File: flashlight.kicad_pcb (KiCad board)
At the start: 2 copper layers, 45 x 120 mm, 23 parts, among them J1 USB_B_Micro, J2 Conn_01x03_Pin, Q2 HSS2333, SW1 SW_DIP_x01, U1 XB4908A, U2 MT3608, U3 TP4057, U4 R6BHC-A05_LED-19-223

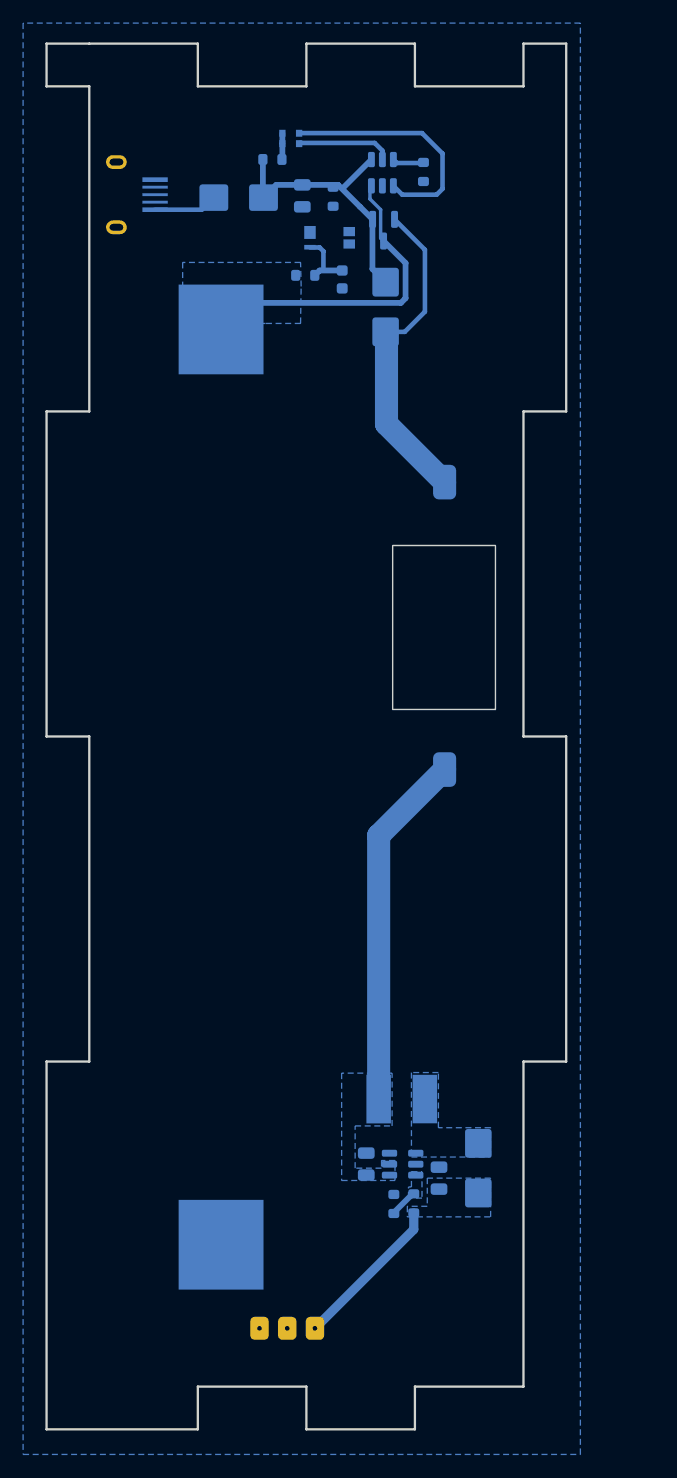
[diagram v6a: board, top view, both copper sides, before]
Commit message: increased 18650 pads size, added led stripe silkscreen line, increased switch hole length by 0.1mm
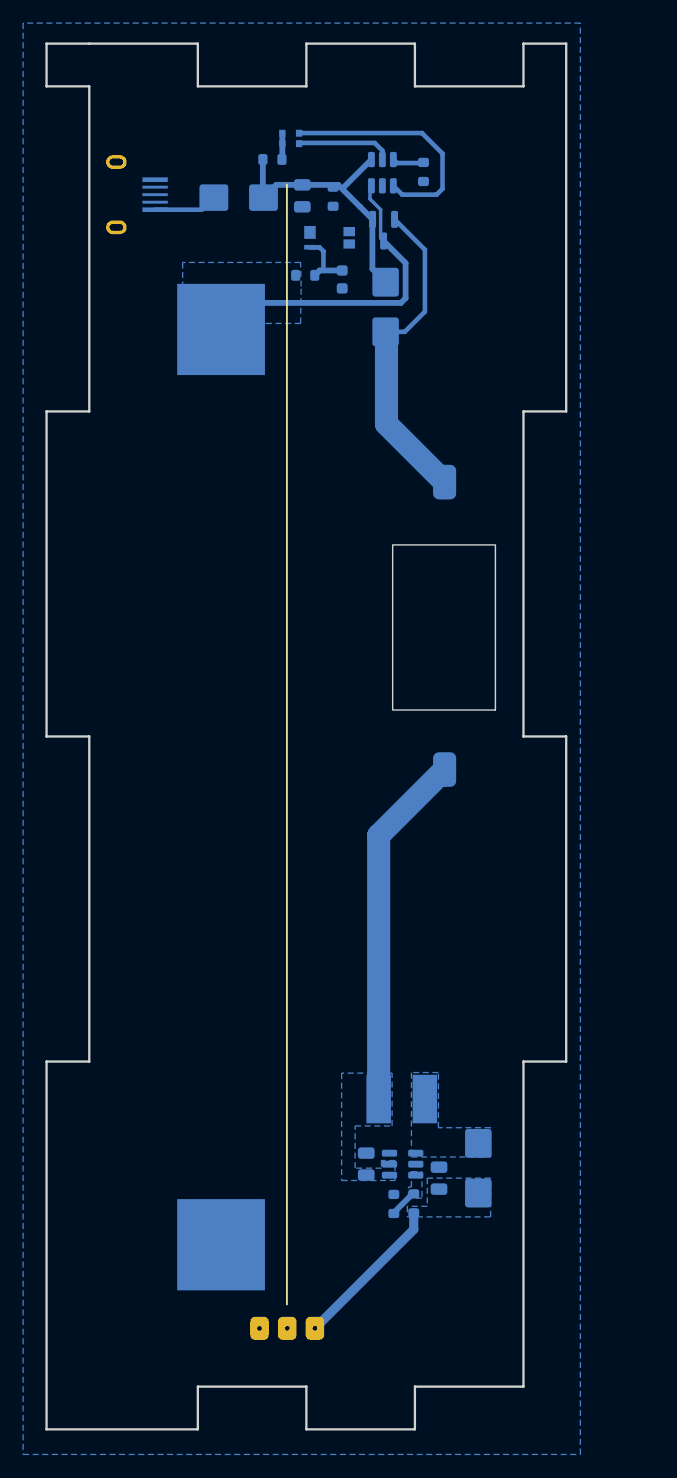
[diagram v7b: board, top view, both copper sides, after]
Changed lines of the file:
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@@
 		)
 		(fp_rect
-			(start 14.1 -8.9)
-			(end -0.1 0)
+			(start 14.15 -8.9)
+			(end -0.15 0)
 			(stroke
 				(width 0.12)
@@
 		(pad "1" smd rect
 			(at 0 -39.63 270)
-			(size 7.77 7.35)
+			(size 7.9 7.6)
 			(layers "B.Cu" "B.Paste" "B.Mask")
 			(net 11 "Net-(BT1-+)")
@@
 		(pad "2" smd rect
 			(at 0 39.63 270)
-			(size 7.77 7.35)
+			(size 7.9 7.6)
 			(layers "B.Cu" "B.Paste" "B.Mask")
 			(net 2 "GND")
@@
 		)
 	)
+	(gr_line
+		(start 96 145)
+		(end 96 48)
+		(stroke
+			(width 0.15)
+			(type default)
+		)
+		(layer "F.SilkS")
+	)
 	(gr_rect

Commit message: xb4908 v2.5
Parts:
- U2: footprint Package_TO_SOT_SMD:SOT-23-6 -> SparkFun-Semiconductor-Standard:SOT23-6-Tight
- moved U1 16.3 mm to (103.1, 68.8), turned to -90 degrees
- moved C2 11.8 mm to (105.7, 67.0), turned to 0 degrees
- moved R3 11.6 mm to (102.9, 66.2), turned to 90 degrees
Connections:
- C3 pad 2: GND -> Earth_Protective
- C4 pad 2: GND -> Earth_Protective
- J2 pad 2: GND -> Earth_Protective
- J2 pad 3: GND -> Earth_Protective
- R6 pad 1: GND -> Earth_Protective
- U1 pad 3: GND -> Earth_Protective
- U1 pad 4: GND -> Earth_Protective
- U2 pad 2: GND -> Earth_Protective
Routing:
- net Net-(U1-VDD): track 5.43 -> 0.00 mm
- net Net-(D4-K): track 28.3 -> 29.9 mm
- added copper zone on B.Cu, net Earth_Protective
- added copper zone on B.Cu, net Net-(U1-VDD)
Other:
- board text added: "V2.5"
- board text removed: "V2.4"
